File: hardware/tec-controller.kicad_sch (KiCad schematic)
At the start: 36 parts, among them U3 MAX1978

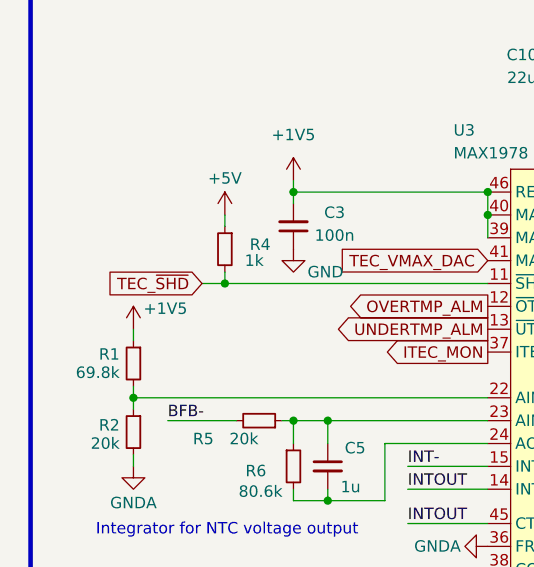
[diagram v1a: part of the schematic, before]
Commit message: feat: syntethizing parser with output registers instead on using external reg, minor fixes to schematic and PCB
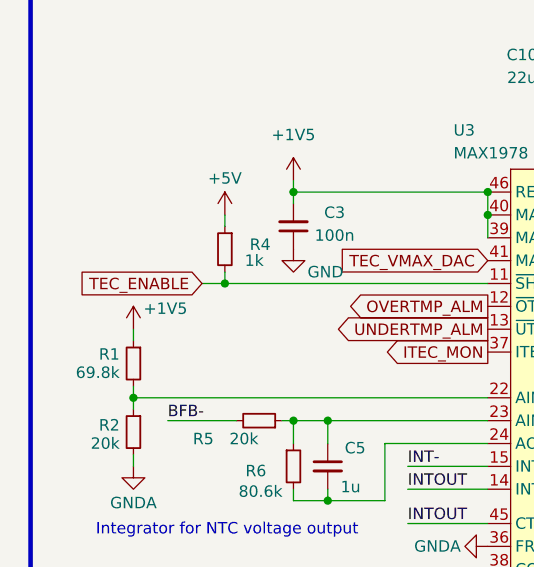
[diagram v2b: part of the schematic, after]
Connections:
- net TEC_~{SHD} renamed TEC_ENABLE
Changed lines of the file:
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@@
 		)
 	)
-	(global_label "TEC_~{SHD}"
+	(global_label "TEC_ENABLE"
 		(shape input)
 		(at 36.83 54.61 180)
@@
 		)
 		(property "Intersheetrefs" "${INTERSHEET_REFS}"
-			(at 25.6806 54.61 0)
+			(at 22.4754 54.61 0)
 			(effects
 				(font
